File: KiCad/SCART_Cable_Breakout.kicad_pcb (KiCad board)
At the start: 2 copper layers, 40 x 25 mm, 17 parts, among them J1 SCART-F, J2 Conn_01x08, U1 ST662A

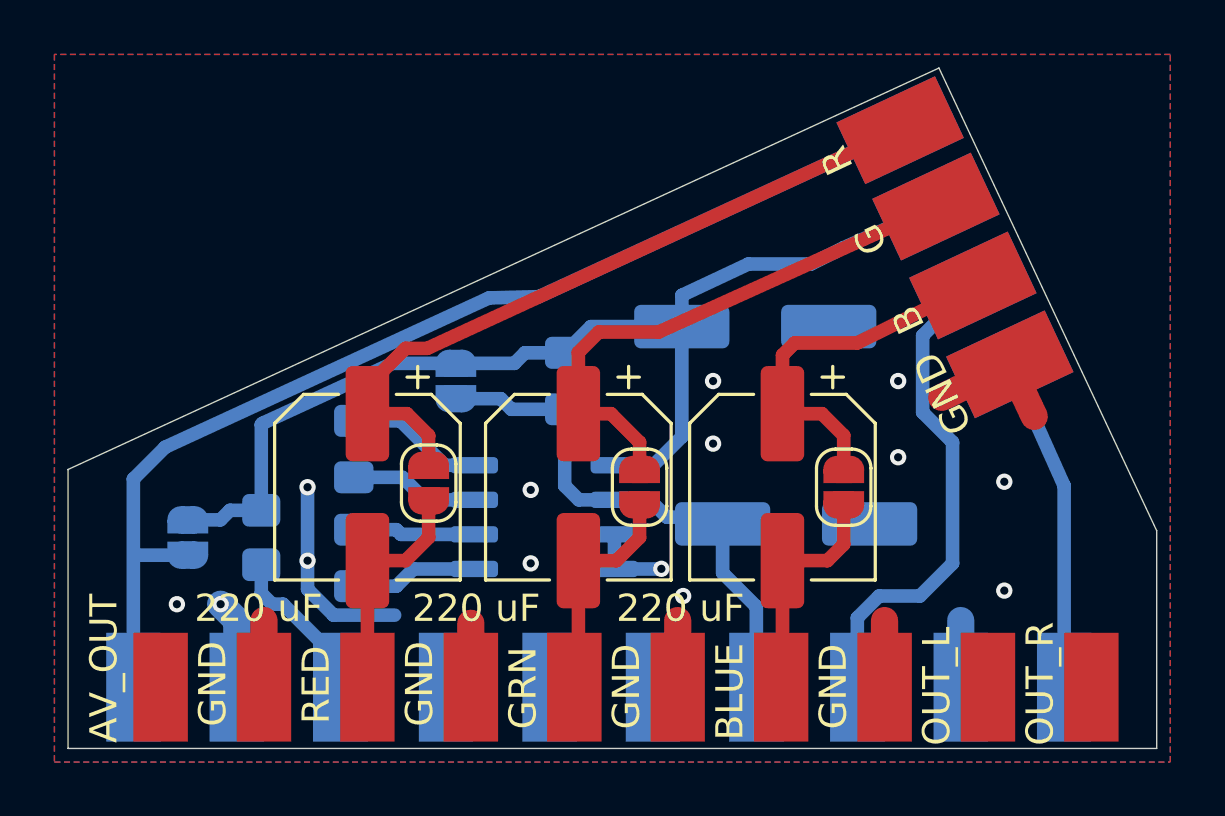
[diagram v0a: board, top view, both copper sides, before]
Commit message: Edit silkscreen labels.
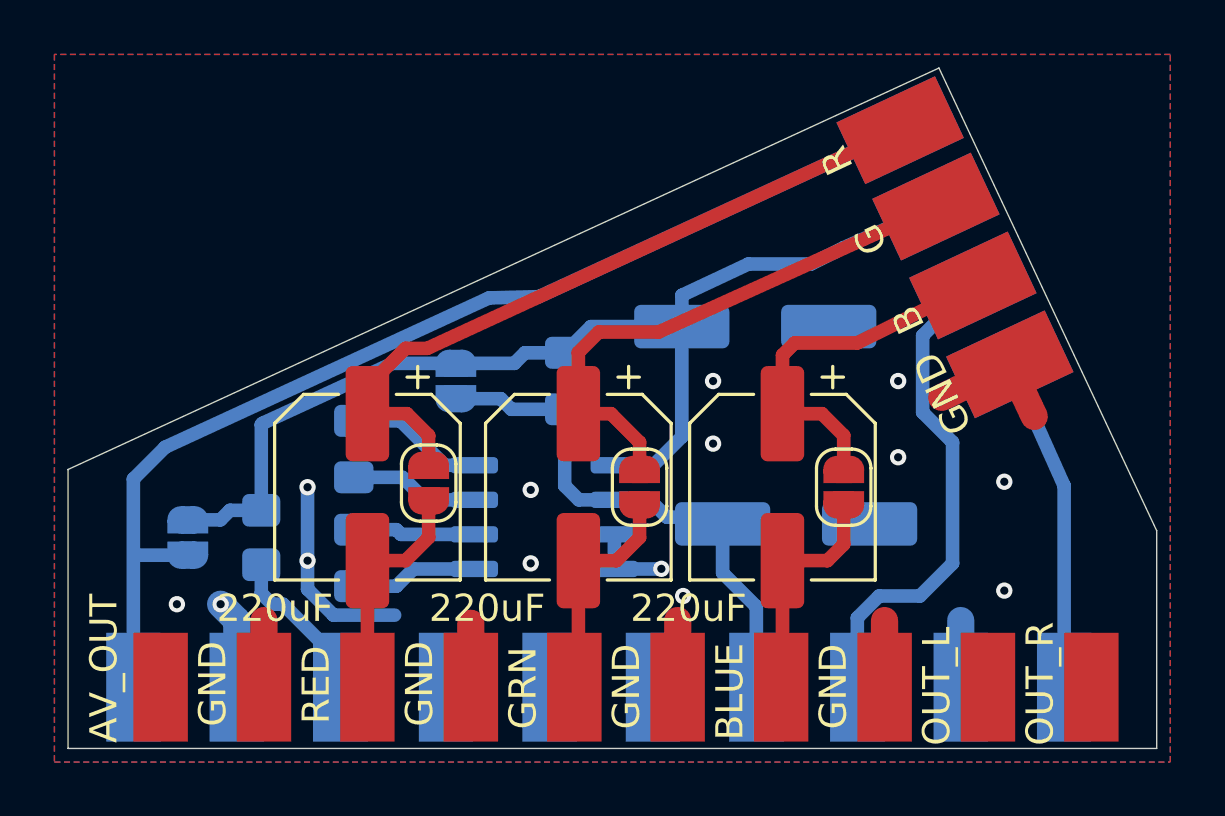
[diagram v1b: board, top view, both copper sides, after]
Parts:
- C1, C2, C3: value 220 uF -> 220uF
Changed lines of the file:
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@@
 			)
 		)
-		(property "Value" "220 uF"
-			(at 4.45 3.75 180)
+		(property "Value" "220uF"
+			(at 4.45 3.35 180)
 			(layer "F.SilkS")
 			(effects
@@
 			)
 		)
-		(property "Value" "220 uF"
-			(at 4.45 4 180)
+		(property "Value" "220uF"
+			(at 4.45 3.4 180)
 			(layer "F.SilkS")
 			(effects
@@
 			)
 		)
-		(property "Value" "220 uF"
-			(at 4.45 3.75 0)
-			(layer "F.SilkS")
-			(effects
+		(property "Value" "220uF"
+			(at 4.45 3.45 0)
+			(layer "F.SilkS")
+			(effects

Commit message: Change PCB outline to match more common SCART connectors. Remove solder jumpers for RGB capacitors. 5V->12V converter: replace electrolytic capacitors with size B tantalum ones.
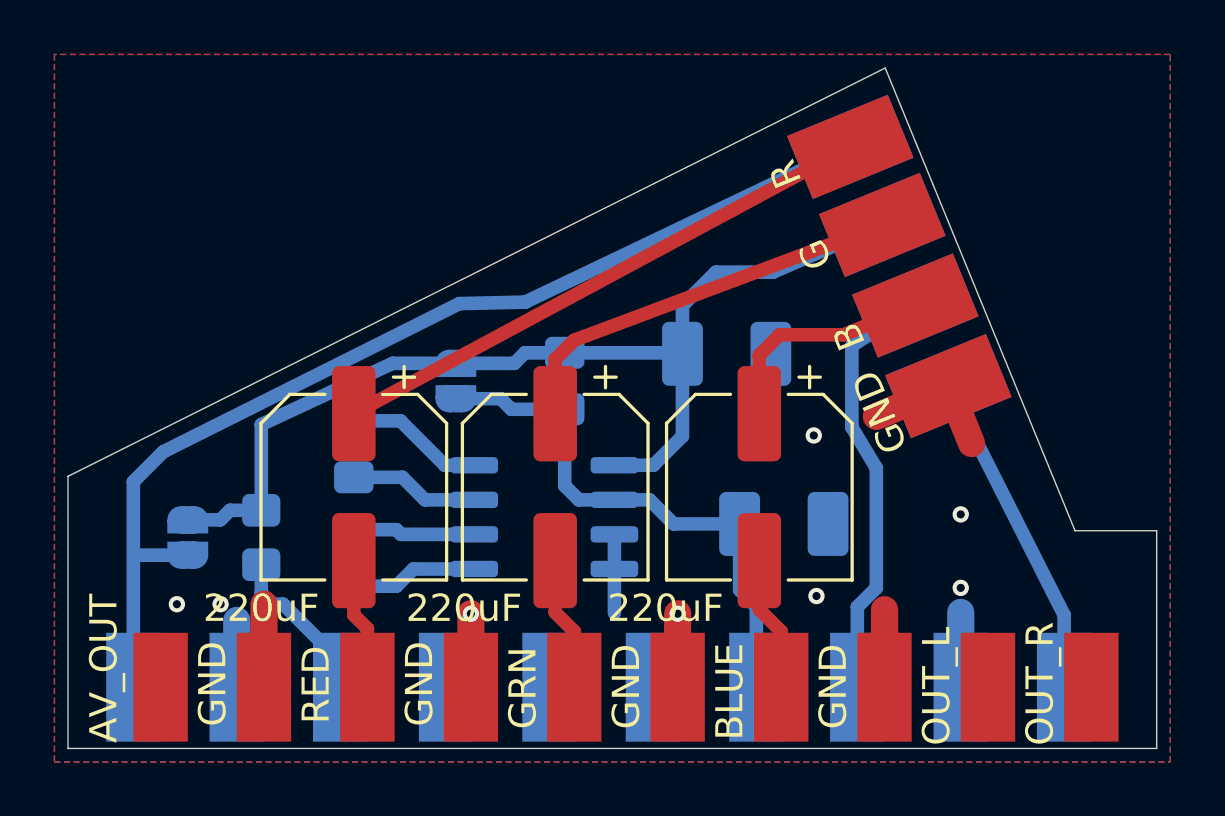
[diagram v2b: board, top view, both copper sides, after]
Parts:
- removed JP1, JP2, JP3: SolderJumper_2_Open, Jumper:SolderJumper-2_P1.3mm_Open_RoundedPad1.0x1.5mm
- C7, C8: footprint Capacitor_SMD:CP_Elec_6.3x3.9 -> Capacitor_Tantalum_SMD:CP_EIA-3528-21_Kemet-B_Pad1.50x2.35mm_HandSolder
- J2: value Conn_01x08 -> SCART Cable
- moved J2 2.28 mm to (97.4, 89.8), turned to 112.3 degrees
- moved C7 1.45 mm to (97.2, 89.0)
- moved C2 0.85 mm to (90.9, 93.9)
- moved C3 0.85 mm to (98.4, 93.9)
- moved C1 0.50 mm to (83.5, 93.9)
- moved C8 0.45 mm to (99.3, 95.2)
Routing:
- net /RED_IN: track 31.3 -> 20.7 mm
- net GND: track 32.1 -> 25.2 mm, vias 14 -> 8
- net /BLUE_IN: track 15.2 -> 8.40 mm
- net /GREEN_IN: track 20.4 -> 15.1 mm
- net /RGB_RED: track 8.60 -> 4.86 mm
- net /RGB_BLUE: track 8.62 -> 5.05 mm
- net /RGB_GREEN: track 8.51 -> 5.15 mm
- net +5V: track 40.7 -> 38.0 mm
- net /AUDIO_IN_L_MONO: track 18.3 -> 15.8 mm
- net /COMPOSITE_VIDEO_IN: track 40.7 -> 38.8 mm
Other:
- outline, holes or cut-outs redrawn
